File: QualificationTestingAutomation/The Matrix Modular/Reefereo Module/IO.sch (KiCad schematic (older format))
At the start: 8 parts, among them J1 Conn_02x32_Counter_Clockwise_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, J2 OBD Connector, J3 OBD Connector, J6 Conn_02x32_Counter_Clockwise_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

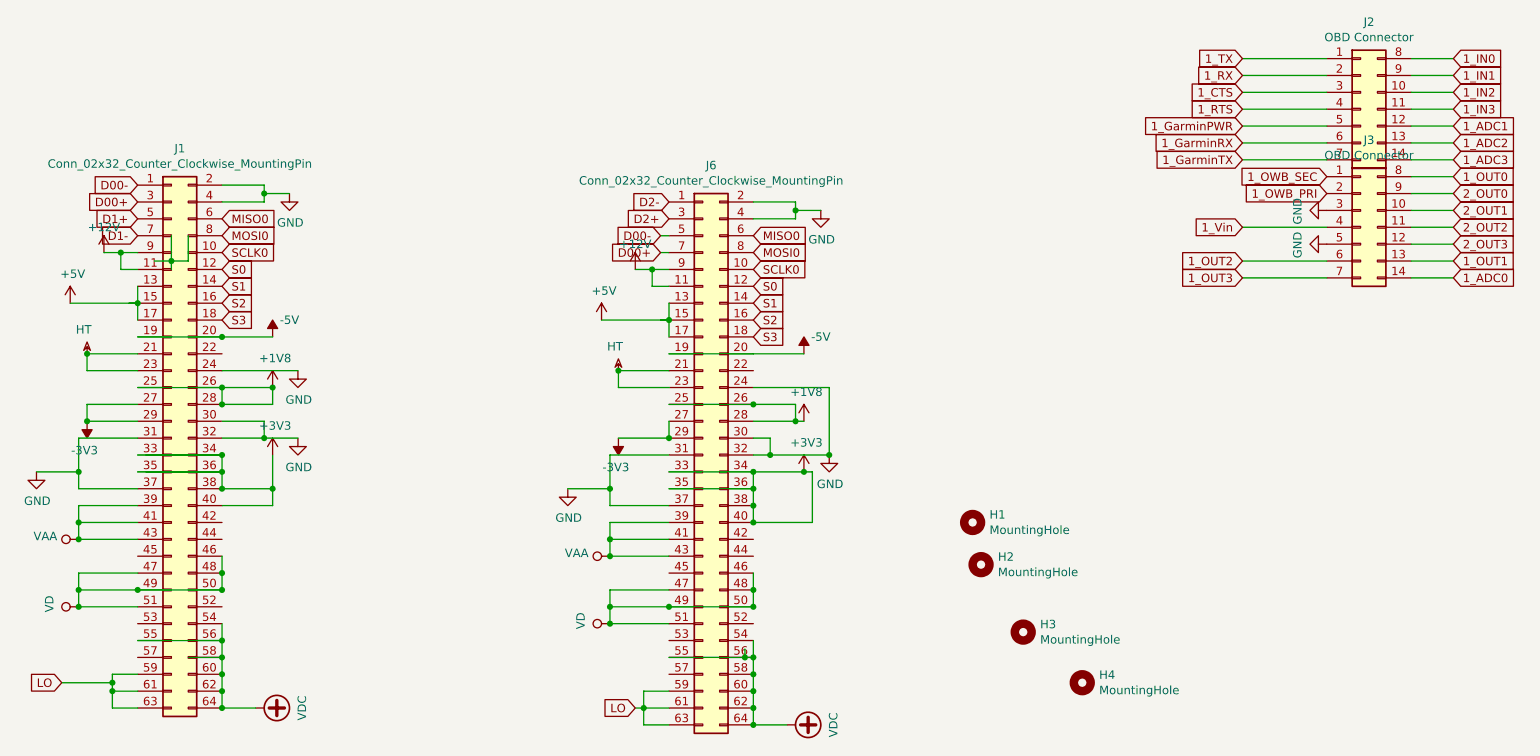
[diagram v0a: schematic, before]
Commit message: Reefero Module PCB design
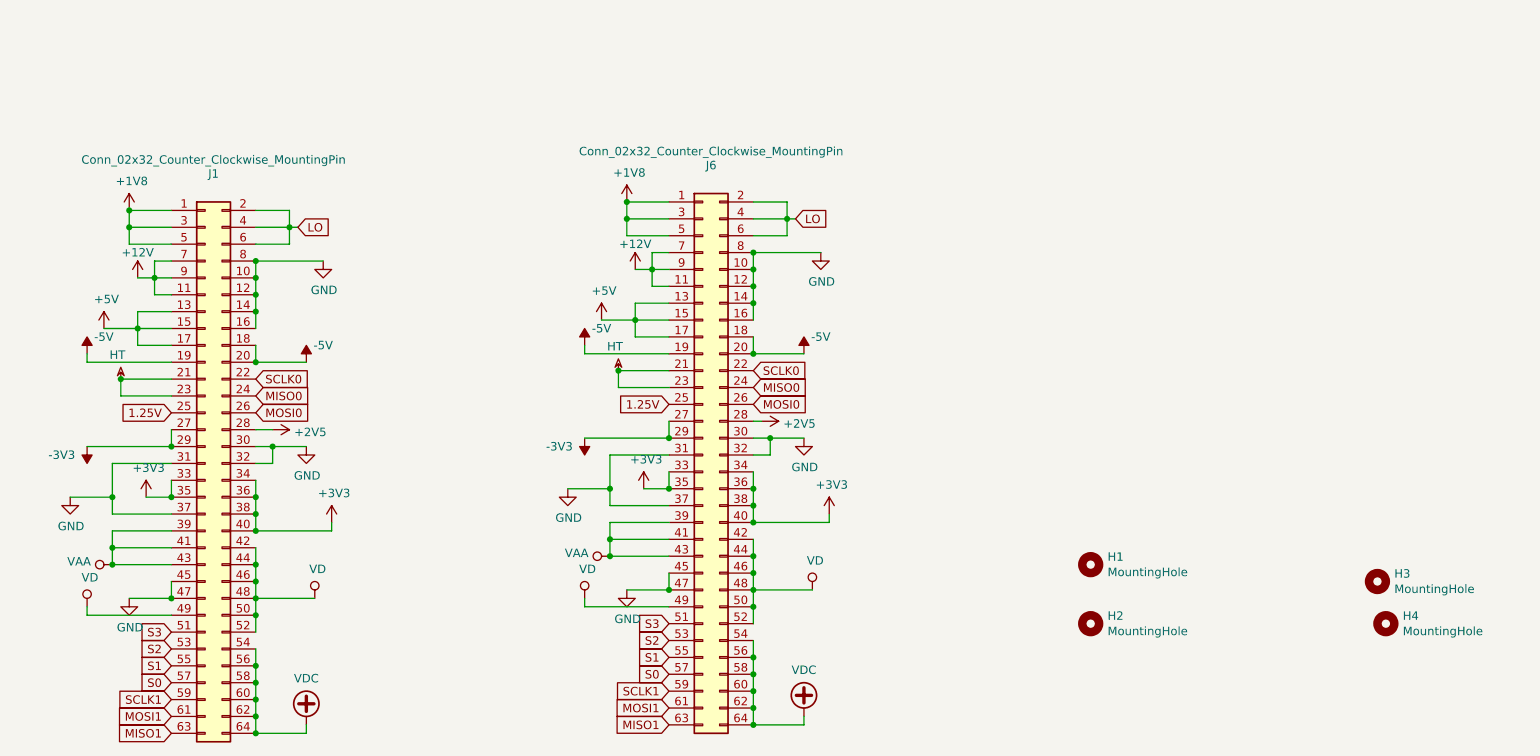
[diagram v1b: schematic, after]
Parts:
- removed J2, J3: OBD Connector, .pretty:3MM, symbol Connector_Generic:Conn_02x07_Top_Bottom
- J1: footprint Connector_PinSocket_2.00mm:PinSocket_2x32_P2.00mm_Horizontal -> Connector:PinHeader_2x32_P2.00mm_VerticalOpp
- J6: footprint Connector_PinHeader_2.00mm:PinHeader_2x32_P2.00mm_Horizontal -> Connector:PinHeader_2x32_P2.00mm_VerticalOpp
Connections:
- net labels added: +2V5, 1.25V, MISO1, MOSI1, SCLK1
- net labels removed: 1_ADC0, 1_ADC1, 1_ADC2, 1_ADC3, 1_CTS, 1_GarminPWR, 1_GarminRX, 1_GarminTX, 1_IN0, 1_IN1, 1_IN2, 1_IN3, 1_OUT0, 1_OUT1, 1_OUT2, 1_OUT3, 1_OWB_PRI, 1_OWB_SEC, 1_RTS, 1_RX, 1_TX, 1_Vin, 2_OUT0, 2_OUT1, 2_OUT2, 2_OUT3, D00+, D00-, D1+, D1-, D2+, D2-
- wire segments 178 -> 152
